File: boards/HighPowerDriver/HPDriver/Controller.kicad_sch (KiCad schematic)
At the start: 20 parts, among them J5 AVR-UPDI-6, U10 74LVC1G123, U11 ATtiny406-S, U12 74AHC1G00, U13 74LVC1G125, U14 74LVC1G125

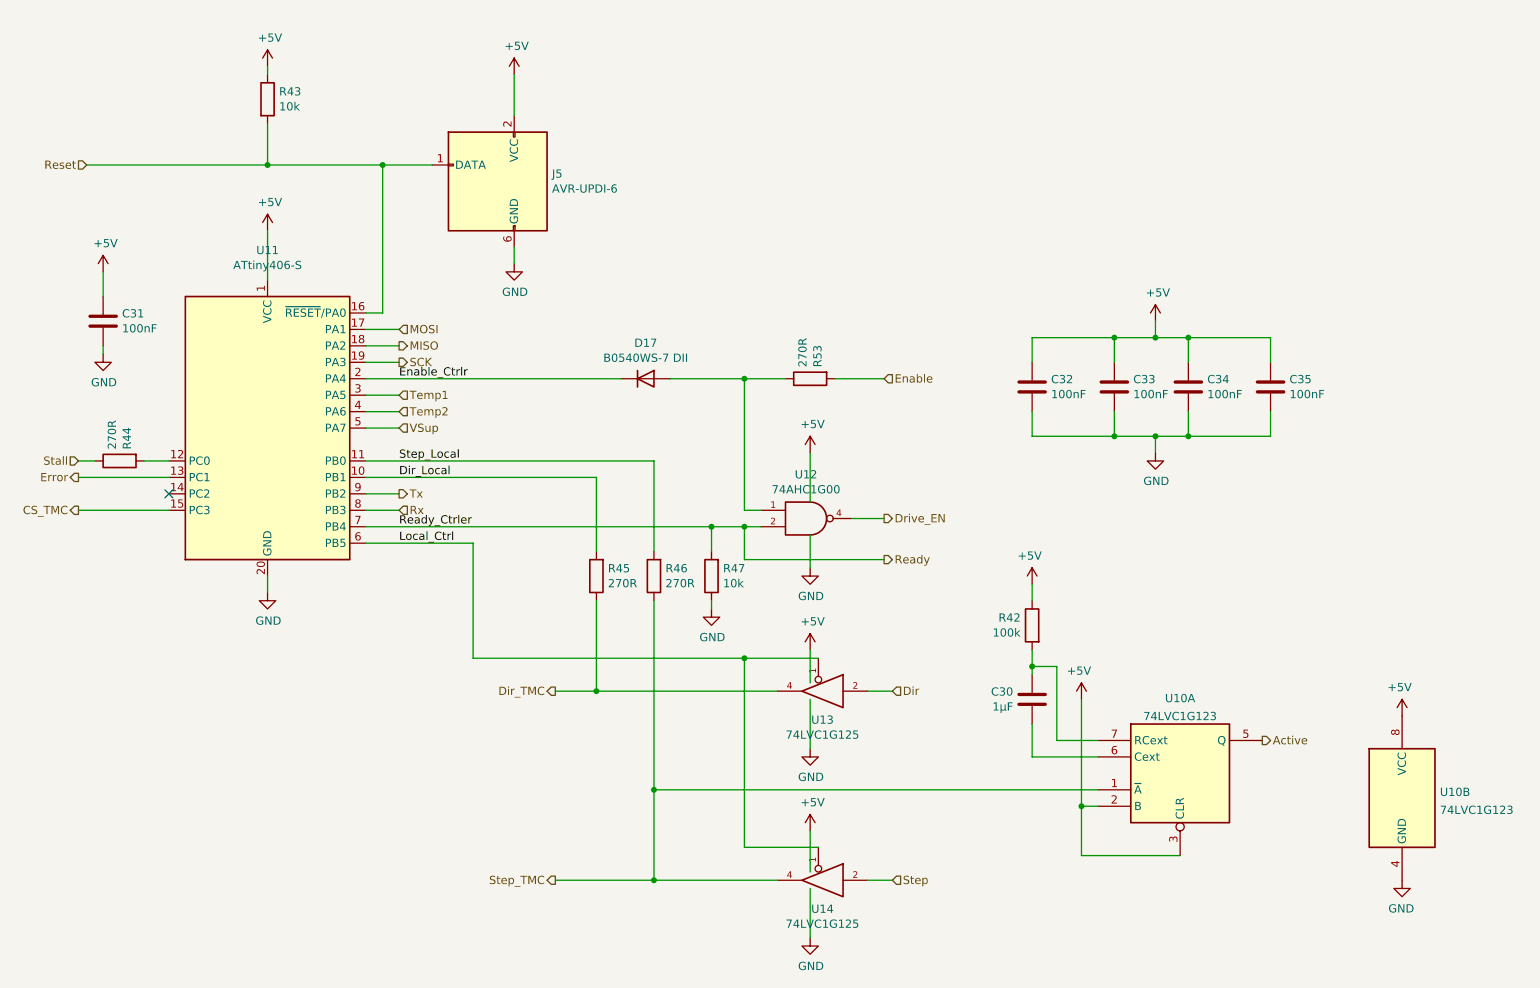
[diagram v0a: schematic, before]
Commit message: Changed Controller to ATmega328PB
The ATtiny did not have enough flash
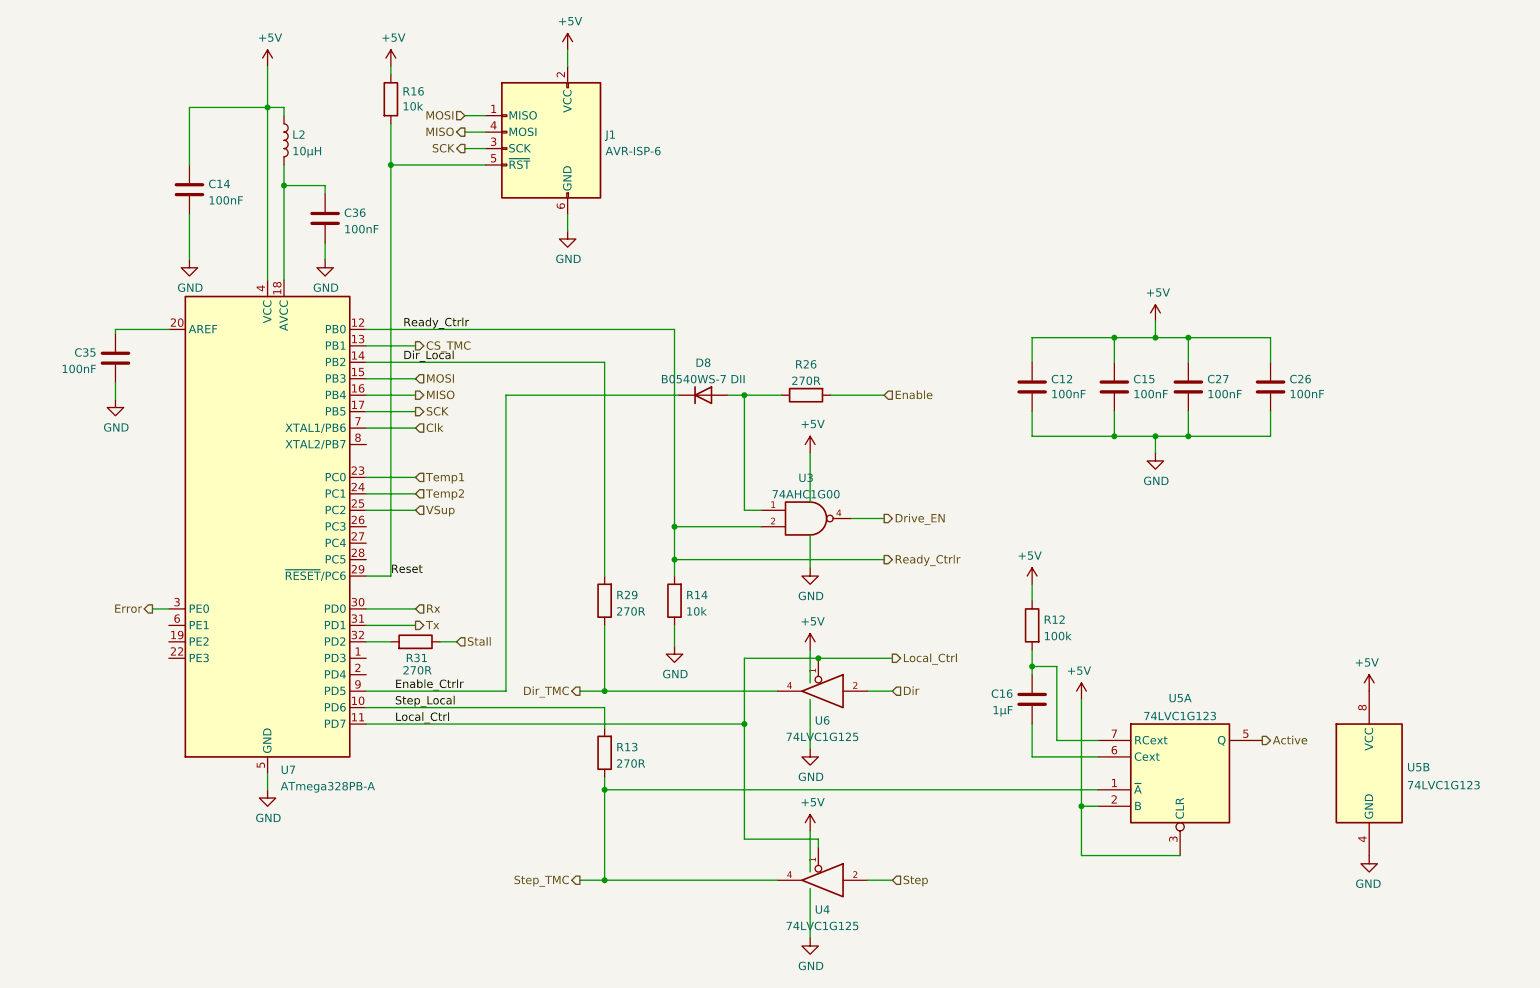
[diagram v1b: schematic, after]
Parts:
- removed J5: AVR-UPDI-6, Connector_IDC:IDC-Header_2x03_P2.54mm_Vertical, symbol Connector:AVR-UPDI-6
- removed U11: ATtiny406-S, Package_SO:SOIC-20W_7.5x12.8mm_P1.27mm, symbol MCU_Microchip_ATtiny:ATtiny406-S
- added C35, C36: 100nF, Capacitor_SMD:C_0805_2012Metric, symbol Device:C
- added J1: AVR-ISP-6, Connector_IDC:IDC-Header_2x03_P2.54mm_Vertical, symbol Connector:AVR-ISP-6
- added L2: 10µH, Inductor_SMD:L_0805_2012Metric, symbol Device:L
- added U7: ATmega328PB-A, Package_QFP:TQFP-32_7x7mm_P0.8mm, symbol MCU_Microchip_ATmega:ATmega328PB-A
- renumbered C32 to C12, C31 to C14, C33 to C15, C30 to C16, C35 to C26, C34 to C27, D17 to D8, R42 to R12, R46 to R13, R47 to R14, R43 to R16, R53 to R26, R45 to R29, R44 to R31, U12 to U3, U14 to U4, U10 to U5, U13 to U6
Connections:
- net +5V: now also J1.2 (VCC), L2.1, U7.4 (VCC)
- net CS_TMC: now also U7.13 (PB1)
- net Dir_Local: now also U7.14 (PB2)
- net Enable_Ctrlr: now also U7.9 (PD5)
- net Error: now also U7.3 (PE0)
- net GND: now also C35.2, C36.2, J1.6 (GND), U7.21 (GND), U7.5 (GND)
- net Local_Ctrl: now also U7.11 (PD7)
- net MISO: now also J1.4 (MOSI), U7.16 (PB4)
- net MOSI: now also J1.1 (MISO), U7.15 (PB3)
- net Reset: now also J1.5 (~{RST}), U7.29 (~{RESET}/PC6)
- net Rx: now also U7.30 (PD0)
- net SCK: now also J1.3 (SCK), U7.17 (PB5)
- net Step_Local: now also U7.10 (PD6)
- net Temp1: now also U7.23 (PC0)
- net Temp2: now also U7.24 (PC1)
- net Tx: now also U7.31 (PD1)
- net VSup: now also U7.25 (PC2)
- net at R31.2: now also U7.32 (PD2)
- net Ready renamed Ready_Ctrlr
- net Ready_Ctrlr: now also U7.12 (PB0)
- new net: C36.1, L2.2, U7.18 (AVCC)
- new net: C35.1, U7.20 (AREF)
- new net Clk: U7.7 (XTAL1/PB6)
- no-connect marks 1 -> 0
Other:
- moved on the sheet: C14, D8, R13, R14, R16, R26, R29, R31, U5B
